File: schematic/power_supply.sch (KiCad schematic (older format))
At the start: 43 parts, among them J1 CONN_01X02, J2 CONN_01X01, J3 CONN_01X01, J4 CONN_01X01, J5 CONN_01X01, J6 CONN_01X01, Q1 Q_PMOS_GSD, U1 MCP1726-3302E/SN, U2 MCP1612, U3 MCP1726-3302E/SN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

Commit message: Updates to schematic, components
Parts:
- C1: footprint (none) -> Capacitors_SMD:C_0805; Voltage 50 -> 25v
- C2: footprint (none) -> Capacitors_SMD:C_0805; Voltage (none) -> 25v
- C3: footprint (none) -> Capacitors_SMD:C_0603
- C4: value 1000pF -> 1nF
- C5: Voltage 50v -> 25v
- C8: value 0.1uF -> 10uF; Voltage (none) -> 25v
- R7: value 12.4k -> 30.9k
- R8: value 10k -> 24.9k
- U2: footprint (none) -> Housings_SSOP:MSOP-8_3x3mm_Pitch0.65mm
- U3: footprint (none) -> Housings_SOIC:SOIC-8_3.9x4.9mm_Pitch1.27mm
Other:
- note added: "Max 5.5v"
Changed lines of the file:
@@
 F 0 "U3" H 7800 1637 60  0000 C CNN
 F 1 "MCP1726-3302E/SN" H 7800 1531 60  0000 C CNN
-F 2 "" H 7750 1200 60  0001 C CNN
+F 2 "Housings_SOIC:SOIC-8_3.9x4.9mm_Pitch1.27mm" H 7750 1200 60  0001 C CNN
 F 3 "" H 7750 1200 60  0001 C CNN
 	1    7800 1200
@@
 F 0 "C2" H 1515 2746 50  0000 L CNN
 F 1 "4.7uF" H 1515 2655 50  0000 L CNN
-F 2 "" H 1438 2550 50  0001 C CNN
+F 2 "Capacitors_SMD:C_0805" H 1438 2550 50  0001 C CNN
 F 3 "" H 1400 2700 50  0001 C CNN
+F 4 "25v" H 1600 2550 60  0000 C CNN "Voltage"
 	1    1400 2700
 	1    0    0    -1
@@
 F 0 "U2" H 2800 5437 60  0000 C CNN
 F 1 "MCP1612" H 2800 5331 60  0000 C CNN
-F 2 "" H 2850 4950 60  0001 C CNN
+F 2 "Housings_SSOP:MSOP-8_3x3mm_Pitch0.65mm" H 2850 4950 60  0001 C CNN
 F 3 "" H 2850 4950 60  0001 C CNN
 	1    2800 4950
@@
 F 0 "C3" H 1865 5196 50  0000 L CNN
 F 1 "0.1uF" H 1865 5105 50  0000 L CNN
-F 2 "" H 1788 5000 50  0001 C CNN
+F 2 "Capacitors_SMD:C_0603" H 1788 5000 50  0001 C CNN
 F 3 "" H 1750 5150 50  0001 C CNN
 	1    1750 5150
@@
 F 0 "C1" H 1365 5249 50  0000 L CNN
 F 1 "10uF" H 1365 5158 50  0000 L CNN
-F 2 "" H 1288 5000 50  0001 C CNN
+F 2 "Capacitors_SMD:C_0805" H 1288 5000 50  0001 C CNN
 F 3 "" H 1250 5150 50  0001 C CNN
-F 4 "50" H 1365 5059 60  0000 L CNN "Voltage"
+F 4 "25v" H 1365 5059 60  0000 L CNN "Voltage"
 	1    1250 5150
 	1    0    0    -1
@@
 P 2200 5750
 F 0 "C4" H 2315 5796 50  0000 L CNN
-F 1 "1000pF" H 2315 5705 50  0000 L CNN
+F 1 "1nF" H 2315 5705 50  0000 L CNN
 F 2 "" H 2238 5600 50  0001 C CNN
 F 3 "" H 2200 5750 50  0001 C CNN
@@
 P 3950 4950
 F 0 "C8" H 4065 4996 50  0000 L CNN
-F 1 "0.1uF" H 4065 4905 50  0000 L CNN
+F 1 "10uF" H 4065 4905 50  0000 L CNN
 F 2 "" H 3988 4800 50  0001 C CNN
 F 3 "" H 3950 4950 50  0001 C CNN
+F 4 "25v" H 4150 4800 60  0000 C CNN "Voltage"
 	1    3950 4950
 	1    0    0    -1
@@
 P 4450 5050
 F 0 "R7" H 4520 5096 50  0000 L CNN
-F 1 "12.4k" H 4520 5005 50  0000 L CNN
+F 1 "30.9k" H 4520 5005 50  0000 L CNN
 F 2 "" V 4380 5050 50  0001 C CNN
 F 3 "" H 4450 5050 50  0001 C CNN
@@
 P 4450 5650
 F 0 "R8" H 4520 5696 50  0000 L CNN
-F 1 "10k" H 4520 5605 50  0000 L CNN
+F 1 "24.9k" H 4520 5605 50  0000 L CNN
 F 2 "" V 4380 5650 50  0001 C CNN
 F 3 "" H 4450 5650 50  0001 C CNN
@@
 F 2 "" H 2638 1300 50  0001 C CNN
 F 3 "" H 2600 1450 50  0001 C CNN
-F 4 "50v" H 2715 1359 60  0000 L CNN "Voltage"
+F 4 "25v" H 2715 1359 60  0000 L CNN "Voltage"
 	1    2600 1450
 	1    0    0    -1
@@
 	3400 2550 3400 2450
 Connection ~ 3400 2450
+Text Notes 1850 850  0    60   ~ 0
+Max 5.5v
 $EndSCHEMATC

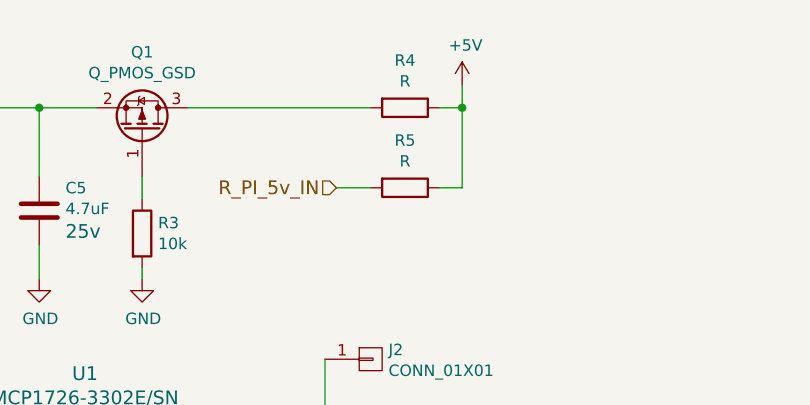
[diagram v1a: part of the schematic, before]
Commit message: Schematic capture almost done. RF layout started.
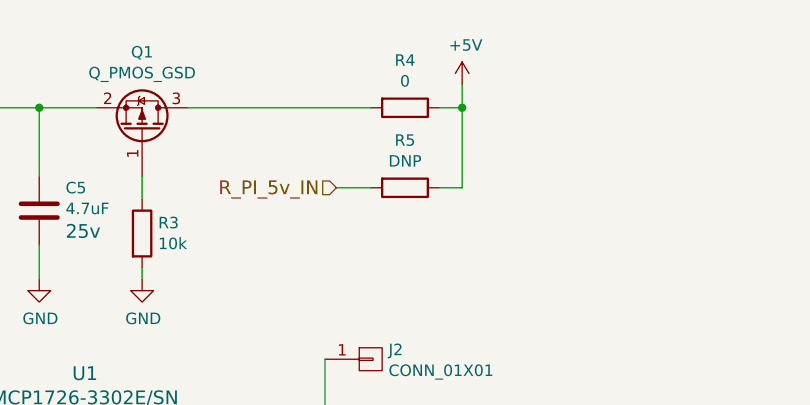
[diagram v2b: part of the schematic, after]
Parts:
- C1, C2: footprint Capacitors_SMD:C_0805 -> Capacitors_SMD:C_0603
- C10, C11, C12, C13, C14, C15, C16, C17, C4, C5, C6, C7, C8, C9: footprint (none) -> Capacitors_SMD:C_0603
- J1: footprint (none) -> Pin_Headers:Pin_Header_Straight_1x02_Pitch2.54mm
- J2, J3, J4, J5, J6: footprint (none) -> SMD_Packages:1Pin
- Q1: footprint (none) -> TO_SOT_Packages_SMD:SOT-23
- R1, R10, R11, R12, R2, R3, R6, R7, R8, R9: footprint (none) -> Resistors_SMD:R_0603
- R4: value R -> 0; footprint (none) -> Resistors_SMD:R_0603
- R5: value R -> DNP; footprint (none) -> Resistors_SMD:R_0603
- U1: footprint (none) -> Housings_SOIC:SOIC-8_3.9x4.9mm_Pitch1.27mm
- U4, U5, U6: footprint (none) -> TO_SOT_Packages_SMD:SOT-23-5
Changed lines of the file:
@@
-EESchema Schematic File Version 2
+EESchema Schematic File Version 3
 LIBS:lohpi-rescue
 LIBS:power
@@
 LIBS:digital-audio
 LIBS:philips
-LIBS:display
 LIBS:cypress
 LIBS:siliconi
@@
 F 0 "U4" H 8075 3087 60  0000 C CNN
 F 1 "MCP1824" H 8075 2981 60  0000 C CNN
-F 2 "" H 8000 2550 60  0001 C CNN
+F 2 "TO_SOT_Packages_SMD:SOT-23-5" H 8000 2550 60  0001 C CNN
 F 3 "" H 8000 2550 60  0001 C CNN
 	1    8100 2700
@@
 F 0 "C12" H 6515 1346 50  0000 L CNN
 F 1 "4.7uF" H 6515 1255 50  0000 L CNN
-F 2 "" H 6438 1150 50  0001 C CNN
+F 2 "Capacitors_SMD:C_0603" H 6438 1150 50  0001 C CNN
 F 3 "" H 6400 1300 50  0001 C CNN
 	1    6400 1300
@@
 F 0 "C14" H 8965 1296 50  0000 L CNN
 F 1 "1.0uF" H 8965 1205 50  0000 L CNN
-F 2 "" H 8888 1100 50  0001 C CNN
+F 2 "Capacitors_SMD:C_0603" H 8888 1100 50  0001 C CNN
 F 3 "" H 8850 1250 50  0001 C CNN
 	1    8850 1250
@@
 F 0 "C13" H 8615 1496 50  0000 L CNN
 F 1 "10nF" H 8615 1405 50  0000 L CNN
-F 2 "" H 8538 1300 50  0001 C CNN
+F 2 "Capacitors_SMD:C_0603" H 8538 1300 50  0001 C CNN
 F 3 "" H 8500 1450 50  0001 C CNN
 	1    8500 1450
@@
 F 0 "C9" H 6465 2796 50  0000 L CNN
 F 1 "4.7uF" H 6465 2705 50  0000 L CNN
-F 2 "" H 6388 2600 50  0001 C CNN
+F 2 "Capacitors_SMD:C_0603" H 6388 2600 50  0001 C CNN
 F 3 "" H 6350 2750 50  0001 C CNN
 	1    6350 2750
@@
 F 0 "C15" H 9015 2846 50  0000 L CNN
 F 1 "1.0uF" H 9015 2755 50  0000 L CNN
-F 2 "" H 8938 2650 50  0001 C CNN
+F 2 "Capacitors_SMD:C_0603" H 8938 2650 50  0001 C CNN
 F 3 "" H 8900 2800 50  0001 C CNN
 	1    8900 2800
@@
 F 0 "U5" H 8075 4437 60  0000 C CNN
 F 1 "MCP1824" H 8075 4331 60  0000 C CNN
-F 2 "" H 8000 3900 60  0001 C CNN
+F 2 "TO_SOT_Packages_SMD:SOT-23-5" H 8000 3900 60  0001 C CNN
 F 3 "" H 8000 3900 60  0001 C CNN
 	1    8100 4050
@@
 F 0 "C10" H 6465 4146 50  0000 L CNN
 F 1 "4.7uF" H 6465 4055 50  0000 L CNN
-F 2 "" H 6388 3950 50  0001 C CNN
+F 2 "Capacitors_SMD:C_0603" H 6388 3950 50  0001 C CNN
 F 3 "" H 6350 4100 50  0001 C CNN
 	1    6350 4100
@@
 F 0 "C16" H 9015 4196 50  0000 L CNN
 F 1 "1.0uF" H 9015 4105 50  0000 L CNN
-F 2 "" H 8938 4000 50  0001 C CNN
+F 2 "Capacitors_SMD:C_0603" H 8938 4000 50  0001 C CNN
 F 3 "" H 8900 4150 50  0001 C CNN
 	1    8900 4150
@@
 F 0 "U6" H 8075 5687 60  0000 C CNN
 F 1 "MCP1824" H 8075 5581 60  0000 C CNN
-F 2 "" H 8000 5150 60  0001 C CNN
+F 2 "TO_SOT_Packages_SMD:SOT-23-5" H 8000 5150 60  0001 C CNN
 F 3 "" H 8000 5150 60  0001 C CNN
 	1    8100 5300
@@
 F 0 "C11" H 6465 5396 50  0000 L CNN
 F 1 "4.7uF" H 6465 5305 50  0000 L CNN
-F 2 "" H 6388 5200 50  0001 C CNN
+F 2 "Capacitors_SMD:C_0603" H 6388 5200 50  0001 C CNN
 F 3 "" H 6350 5350 50  0001 C CNN
 	1    6350 5350
@@
 F 0 "C17" H 9015 5446 50  0000 L CNN
 F 1 "1.0uF" H 9015 5355 50  0000 L CNN
-F 2 "" H 8938 5250 50  0001 C CNN
+F 2 "Capacitors_SMD:C_0603" H 8938 5250 50  0001 C CNN
 F 3 "" H 8900 5400 50  0001 C CNN
 	1    8900 5400
@@
 P 4200 1000
 F 0 "R4" V 3993 1000 50  0000 C CNN
-F 1 "R" V 4084 1000 50  0000 C CNN
-F 2 "" V 4130 1000 50  0001 C CNN
+F 1 "0" V 4084 1000 50  0000 C CNN
+F 2 "Resistors_SMD:R_0603" V 4130 1000 50  0001 C CNN
 F 3 "" H 4200 1000 50  0001 C CNN
 	1    4200 1000
@@
 P 4200 1350
 F 0 "R5" V 3993 1350 50  0000 C CNN
-F 1 "R" V 4084 1350 50  0000 C CNN
-F 2 "" V 4130 1350 50  0001 C CNN
+F 1 "DNP" V 4084 1350 50  0000 C CNN
+F 2 "Resistors_SMD:R_0603" V 4130 1350 50  0001 C CNN
 F 3 "" H 4200 1350 50  0001 C CNN
 	1    4200 1350
@@
 F 0 "U1" H 2800 3037 60  0000 C CNN
 F 1 "MCP1726-3302E/SN" H 2800 2931 60  0000 C CNN
-F 2 "" H 2750 2600 60  0001 C CNN
+F 2 "Housings_SOIC:SOIC-8_3.9x4.9mm_Pitch1.27mm" H 2750 2600 60  0001 C CNN
 F 3 "" H 2750 2600 60  0001 C CNN
 	1    2800 2600
@@
 F 0 "C2" H 1515 2746 50  0000 L CNN
 F 1 "4.7uF" H 1515 2655 50  0000 L CNN
-F 2 "Capacitors_SMD:C_0805" H 1438 2550 50  0001 C CNN
+F 2 "Capacitors_SMD:C_0603" H 1438 2550 50  0001 C CNN
 F 3 "" H 1400 2700 50  0001 C CNN
 F 4 "25v" H 1600 2550 60  0000 C CNN "Voltage"
@@
 F 0 "C7" H 3965 2696 50  0000 L CNN
 F 1 "1.0uF" H 3965 2605 50  0000 L CNN
-F 2 "" H 3888 2500 50  0001 C CNN
+F 2 "Capacitors_SMD:C_0603" H 3888 2500 50  0001 C CNN
 F 3 "" H 3850 2650 50  0001 C CNN
 	1    3850 2650
@@
 F 0 "C6" H 3615 2896 50  0000 L CNN
 F 1 "10nF" H 3615 2805 50  0000 L CNN
-F 2 "" H 3538 2700 50  0001 C CNN
+F 2 "Capacitors_SMD:C_0603" H 3538 2700 50  0001 C CNN
 F 3 "" H 3500 2850 50  0001 C CNN
 	1    3500 2850
@@
 F 0 "J3" H 9128 741 50  0000 L CNN
 F 1 "CONN_01X01" H 9128 650 50  0000 L CNN
-F 2 "" H 9050 700 50  0001 C CNN
+F 2 "SMD_Packages:1Pin" H 9050 700 50  0001 C CNN
 F 3 "" H 9050 700 50  0001 C CNN
 	1    9050 700
@@
 F 0 "J4" H 9178 2291 50  0000 L CNN
 F 1 "CONN_01X01" H 9178 2200 50  0000 L CNN
-F 2 "" H 9100 2250 50  0001 C CNN
+F 2 "SMD_Packages:1Pin" H 9100 2250 50  0001 C CNN
 F 3 "" H 9100 2250 50  0001 C CNN
 	1    9100 2250
@@
 F 0 "J5" H 9178 3691 50  0000 L CNN
 F 1 "CONN_01X01" H 9178 3600 50  0000 L CNN
-F 2 "" H 9100 3650 50  0001 C CNN
+F 2 "SMD_Packages:1Pin" H 9100 3650 50  0001 C CNN
 F 3 "" H 9100 3650 50  0001 C CNN
 	1    9100 3650
@@
 F 0 "J6" H 9178 4941 50  0000 L CNN
 F 1 "CONN_01X01" H 9178 4850 50  0000 L CNN
-F 2 "" H 9100 4900 50  0001 C CNN
+F 2 "SMD_Packages:1Pin" H 9100 4900 50  0001 C CNN
 F 3 "" H 9100 4900 50  0001 C CNN
 	1    9100 4900
@@
 F 0 "J2" H 4128 2141 50  0000 L CNN
 F 1 "CONN_01X01" H 4128 2050 50  0000 L CNN
-F 2 "" H 4050 2100 50  0001 C CNN
+F 2 "SMD_Packages:1Pin" H 4050 2100 50  0001 C CNN
 F 3 "" H 4050 2100 50  0001 C CNN
 	1    4050 2100
@@
 F 0 "R1" V 1807 4900 50  0000 C CNN
 F 1 "10" V 1716 4900 50  0000 C CNN
-F 2 "" V 1530 4900 50  0001 C CNN
+F 2 "Resistors_SMD:R_0603" V 1530 4900 50  0001 C CNN
 F 3 "" H 1600 4900 50  0001 C CNN
 	1    1600 4900
@@
 F 0 "C1" H 1365 5249 50  0000 L CNN
 F 1 "10uF" H 1365 5158 50  0000 L CNN
-F 2 "Capacitors_SMD:C_0805" H 1288 5000 50  0001 C CNN
+F 2 "Capacitors_SMD:C_0603" H 1288 5000 50  0001 C CNN
 F 3 "" H 1250 5150 50  0001 C CNN
 F 4 "25v" H 1365 5059 60  0000 L CNN "Voltage"
@@
 F 0 "C4" H 2315 5796 50  0000 L CNN
 F 1 "1nF" H 2315 5705 50  0000 L CNN
-F 2 "" H 2238 5600 50  0001 C CNN
+F 2 "Capacitors_SMD:C_0603" H 2238 5600 50  0001 C CNN
 F 3 "" H 2200 5750 50  0001 C CNN
 	1    2200 5750
@@
 F 0 "R2" H 2270 5396 50  0000 L CNN
 F 1 "24.9k" H 2270 5305 50  0000 L CNN
-F 2 "" V 2130 5350 50  0001 C CNN
+F 2 "Resistors_SMD:R_0603" V 2130 5350 50  0001 C CNN
 F 3 "" H 2200 5350 50  0001 C CNN
 	1    2200 5350
@@
 F 0 "C8" H 4065 4996 50  0000 L CNN
 F 1 "10uF" H 4065 4905 50  0000 L CNN
-F 2 "" H 3988 4800 50  0001 C CNN
+F 2 "Capacitors_SMD:C_0603" H 3988 4800 50  0001 C CNN
 F 3 "" H 3950 4950 50  0001 C CNN
 F 4 "25v" H 4150 4800 60  0000 C CNN "Voltage"
@@
 F 0 "R7" H 4520 5096 50  0000 L CNN
 F 1 "30.9k" H 4520 5005 50  0000 L CNN
-F 2 "" V 4380 5050 50  0001 C CNN
+F 2 "Resistors_SMD:R_0603" V 4380 5050 50  0001 C CNN
 F 3 "" H 4450 5050 50  0001 C CNN
 	1    4450 5050
@@
 F 0 "R8" H 4520 5696 50  0000 L CNN
 F 1 "24.9k" H 4520 5605 50  0000 L CNN
-F 2 "" V 4380 5650 50  0001 C CNN
+F 2 "Resistors_SMD:R_0603" V 4380 5650 50  0001 C CNN
 F 3 "" H 4450 5650 50  0001 C CNN
 	1    4450 5650
@@
 F 0 "Q1" V 3393 1100 50  0000 C CNN
 F 1 "Q_PMOS_GSD" V 3302 1100 50  0000 C CNN
-F 2 "" H 3250 1200 50  0001 C CNN
+F 2 "TO_SOT_Packages_SMD:SOT-23" H 3250 1200 50  0001 C CNN
 F 3 "" H 3050 1100 50  0001 C CNN
 	1    3050 1100
@@
 F 0 "R3" H 3120 1596 50  0000 L CNN
 F 1 "10k" H 3120 1505 50  0000 L CNN
-F 2 "" V 2980 1550 50  0001 C CNN
+F 2 "Resistors_SMD:R_0603" V 2980 1550 50  0001 C CNN
 F 3 "" H 3050 1550 50  0001 C CNN
 	1    3050 1550
@@
 F 0 "C5" H 2715 1549 50  0000 L CNN
 F 1 "4.7uF" H 2715 1458 50  0000 L CNN
-F 2 "" H 2638 1300 50  0001 C CNN
+F 2 "Capacitors_SMD:C_0603" H 2638 1300 50  0001 C CNN
 F 3 "" H 2600 1450 50  0001 C CNN
 F 4 "25v" H 2715 1359 60  0000 L CNN "Voltage"
@@
 F 0 "J1" H 1928 1091 50  0000 L CNN
 F 1 "CONN_01X02" H 1928 1000 50  0000 L CNN
-F 2 "" H 1850 1050 50  0001 C CNN
+F 2 "Pin_Headers:Pin_Header_Straight_1x02_Pitch2.54mm" H 1850 1050 50  0001 C CNN
 F 3 "" H 1850 1050 50  0001 C CNN
 	1    1850 1050
@@
 F 0 "R9" V 9100 1000 50  0000 C CNN
 F 1 "0" V 9200 1050 50  0000 C CNN
-F 2 "" V 9130 1050 50  0001 C CNN
+F 2 "Resistors_SMD:R_0603" V 9130 1050 50  0001 C CNN
 F 3 "" H 9200 1050 50  0001 C CNN
 	1    9200 1050
@@
 F 0 "R10" V 9150 2600 50  0000 C CNN
 F 1 "0" V 9250 2600 50  0000 C CNN
-F 2 "" V 9180 2600 50  0001 C CNN
+F 2 "Resistors_SMD:R_0603" V 9180 2600 50  0001 C CNN
 F 3 "" H 9250 2600 50  0001 C CNN
 	1    9250 2600
@@
 F 0 "R11" V 9150 3950 50  0000 C CNN
 F 1 "0" V 9250 3950 50  0000 C CNN
-F 2 "" V 9180 3950 50  0001 C CNN
+F 2 "Resistors_SMD:R_0603" V 9180 3950 50  0001 C CNN
 F 3 "" H 9250 3950 50  0001 C CNN
 	1    9250 3950
@@
 F 0 "R12" V 9150 5200 50  0000 C CNN
 F 1 "0" V 9250 5200 50  0000 C CNN
-F 2 "" V 9180 5200 50  0001 C CNN
+F 2 "Resistors_SMD:R_0603" V 9180 5200 50  0001 C CNN
 F 3 "" H 9250 5200 50  0001 C CNN
 	1    9250 5200
@@
 F 0 "R6" V 4100 2450 50  0000 C CNN
 F 1 "0" V 4200 2450 50  0000 C CNN
-F 2 "" V 4130 2450 50  0001 C CNN
+F 2 "Resistors_SMD:R_0603" V 4130 2450 50  0001 C CNN
 F 3 "" H 4200 2450 50  0001 C CNN
 	1    4200 2450

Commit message: RF layout updated. Rest still needs work
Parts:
- L1: footprint (none) -> Inductors_SMD:L_0603
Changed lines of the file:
@@
 LIBS:digital-audio
 LIBS:philips
+LIBS:display
 LIBS:cypress
 LIBS:siliconi
@@
 F 0 "L1" V 3750 4800 50  0000 C CNN
 F 1 "3.3uH" V 3650 4900 50  0000 C CNN
-F 2 "" H 3550 4800 50  0001 C CNN
+F 2 "Inductors_SMD:L_0603" H 3550 4800 50  0001 C CNN
 F 3 "" H 3550 4800 50  0001 C CNN
 F 4 "1A" V 3650 4650 60  0000 C CNN "I"

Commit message: PCB layout finished, needs review
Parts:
- added C84, C85, C86, C87, C89, C90, C91: 1.0uF, Capacitors_SMD:C_0603, symbol C
- added L10, L11, L12, L13, L9: 2.2uH, Inductors_SMD:L_0805, symbol L
- J2, J3, J4, J5, J6: footprint SMD_Packages:1Pin -> Pin_Headers:Pin_Header_Straight_1x01_Pitch2.54mm
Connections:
- net GND: now also C84.2, C85.2, C86.2, C87.2, C89.2, C90.2, C91.2
- net VCC_3.3v: now also L9.2; no longer R6.1
- net VCC_LNA_A: now also C90.1, L13.2; no longer R12.1
- net VCC_PA: now also C91.1, L10.2; no longer R9.1
- net VCC_RADIO_A: now also L11.2; no longer R10.1
- net VCC_RADIO_B: now also C89.1, L12.2; no longer R11.1
- new net: C87.1, L10.1, R9.1
- new net: C84.1, L11.1, R10.1
- new net: C85.1, L12.1, R11.1
- new net: C86.1, L13.1, R12.1
- new net: L9.1, R6.1

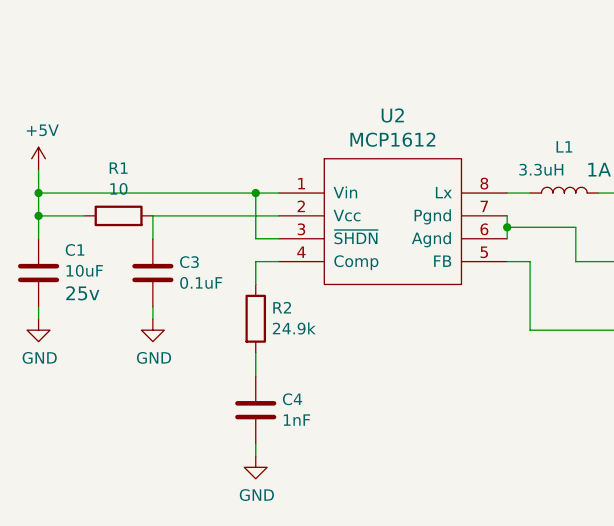
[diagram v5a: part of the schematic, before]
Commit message: Layout approaching final version. BOM updated
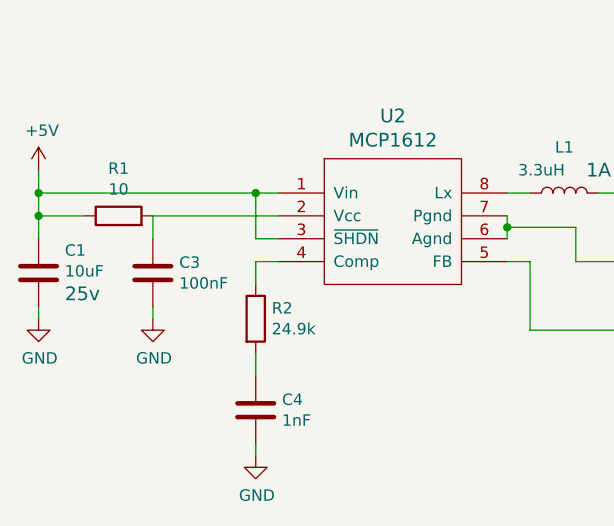
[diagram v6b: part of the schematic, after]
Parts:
- C13, C6: footprint Capacitors_SMD:C_0603 -> Capacitors_SMD:C_0402_NoSilk
- C3: value 0.1uF -> 100nF
- R1: footprint Resistors_SMD:R_0603 -> Resistors_SMD:R_0402_NoSilk
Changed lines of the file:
@@
 F 0 "C13" H 8615 1496 50  0000 L CNN
 F 1 "10nF" H 8615 1405 50  0000 L CNN
-F 2 "Capacitors_SMD:C_0603" H 8538 1300 50  0001 C CNN
+F 2 "Capacitors_SMD:C_0402_NoSilk" H 8538 1300 50  0001 C CNN
 F 3 "" H 8500 1450 50  0001 C CNN
 	1    8500 1450
@@
 F 0 "C6" H 3615 2896 50  0000 L CNN
 F 1 "10nF" H 3615 2805 50  0000 L CNN
-F 2 "Capacitors_SMD:C_0603" H 3538 2700 50  0001 C CNN
+F 2 "Capacitors_SMD:C_0402_NoSilk" H 3538 2700 50  0001 C CNN
 F 3 "" H 3500 2850 50  0001 C CNN
 	1    3500 2850
@@
 F 0 "R1" V 1807 4900 50  0000 C CNN
 F 1 "10" V 1716 4900 50  0000 C CNN
-F 2 "Resistors_SMD:R_0603" V 1530 4900 50  0001 C CNN
+F 2 "Resistors_SMD:R_0402_NoSilk" V 1530 4900 50  0001 C CNN
 F 3 "" H 1600 4900 50  0001 C CNN
 	1    1600 4900
@@
 P 1750 5150
 F 0 "C3" H 1865 5196 50  0000 L CNN
-F 1 "0.1uF" H 1865 5105 50  0000 L CNN
+F 1 "100nF" H 1865 5105 50  0000 L CNN
 F 2 "Capacitors_SMD:C_0603" H 1788 5000 50  0001 C CNN
 F 3 "" H 1750 5150 50  0001 C CNN

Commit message: Add the rest of the passive components to bom
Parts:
- L1: footprint Inductors_SMD:L_0603 -> Inductors_SMD:L_0805
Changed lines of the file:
@@
 F 0 "L1" V 3750 4800 50  0000 C CNN
 F 1 "3.3uH" V 3650 4900 50  0000 C CNN
-F 2 "Inductors_SMD:L_0603" H 3550 4800 50  0001 C CNN
+F 2 "Inductors_SMD:L_0805" H 3550 4800 50  0001 C CNN
 F 3 "" H 3550 4800 50  0001 C CNN
 F 4 "1A" V 3650 4650 60  0000 C CNN "I"

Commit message: Correct component for SMPS inductor, changed footprint
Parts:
- L1: footprint Inductors_SMD:L_0805 -> 84332C:84332C
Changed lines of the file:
@@
 LIBS:power
 LIBS:device
-LIBS:transistors
-LIBS:conn
 LIBS:linear
 LIBS:regul
-LIBS:74xx
-LIBS:cmos4000
 LIBS:adc-dac
 LIBS:memory
@@
 LIBS:digital-audio
 LIBS:philips
-LIBS:display
 LIBS:cypress
 LIBS:siliconi
@@
 LIBS:atmel
 LIBS:contrib
-LIBS:valves
 LIBS:semtech_parts
 LIBS:raspberry_pi
@@
 F 0 "L1" V 3750 4800 50  0000 C CNN
 F 1 "3.3uH" V 3650 4900 50  0000 C CNN
-F 2 "Inductors_SMD:L_0805" H 3550 4800 50  0001 C CNN
+F 2 "84332C:84332C" H 3550 4800 50  0001 C CNN
 F 3 "" H 3550 4800 50  0001 C CNN
 F 4 "1A" V 3650 4650 60  0000 C CNN "I"
